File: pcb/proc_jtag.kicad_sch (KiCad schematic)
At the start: 3 parts

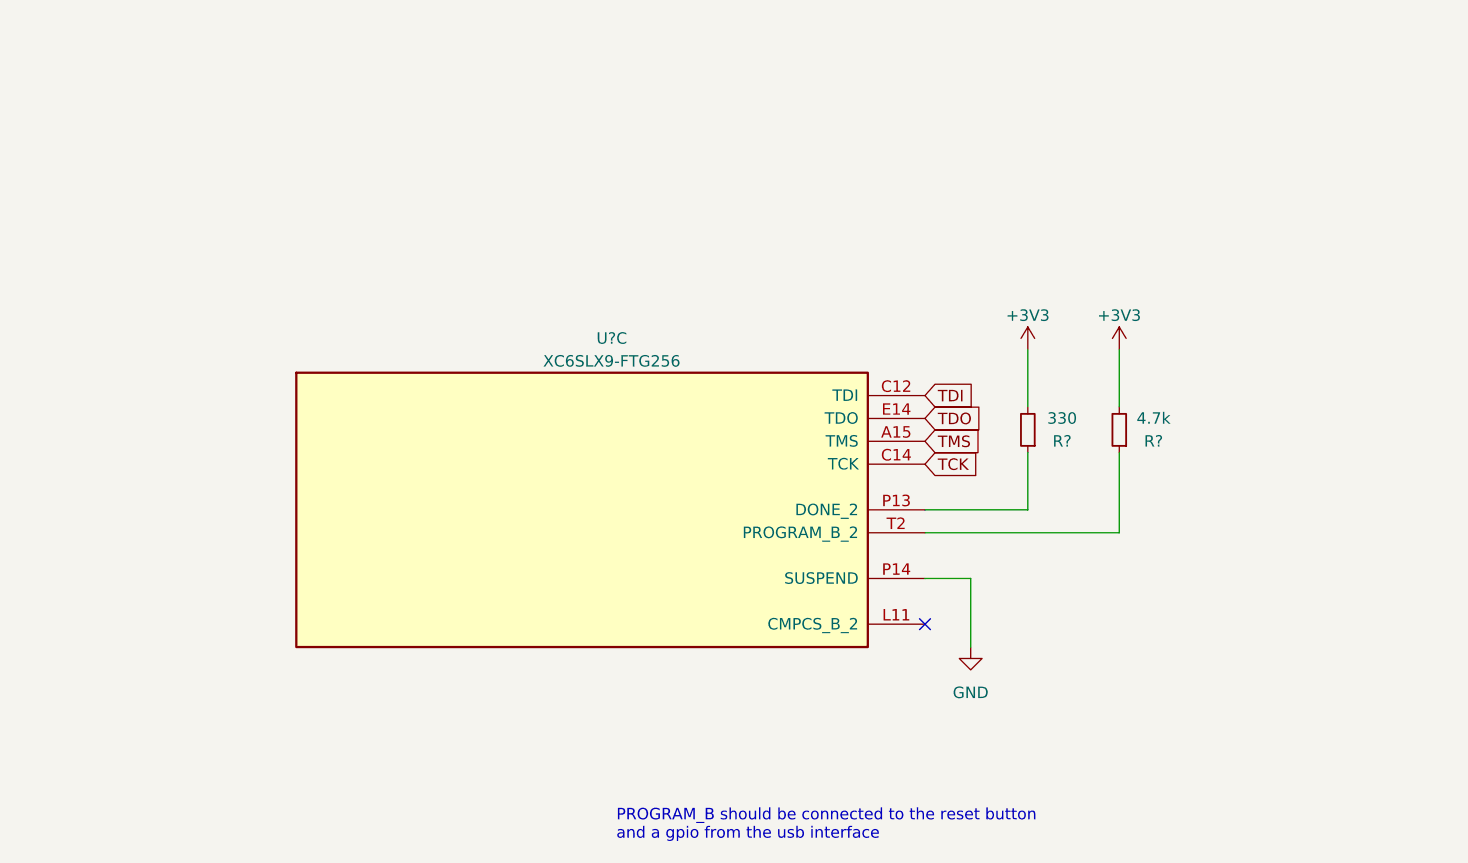
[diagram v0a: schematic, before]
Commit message: add flash memory
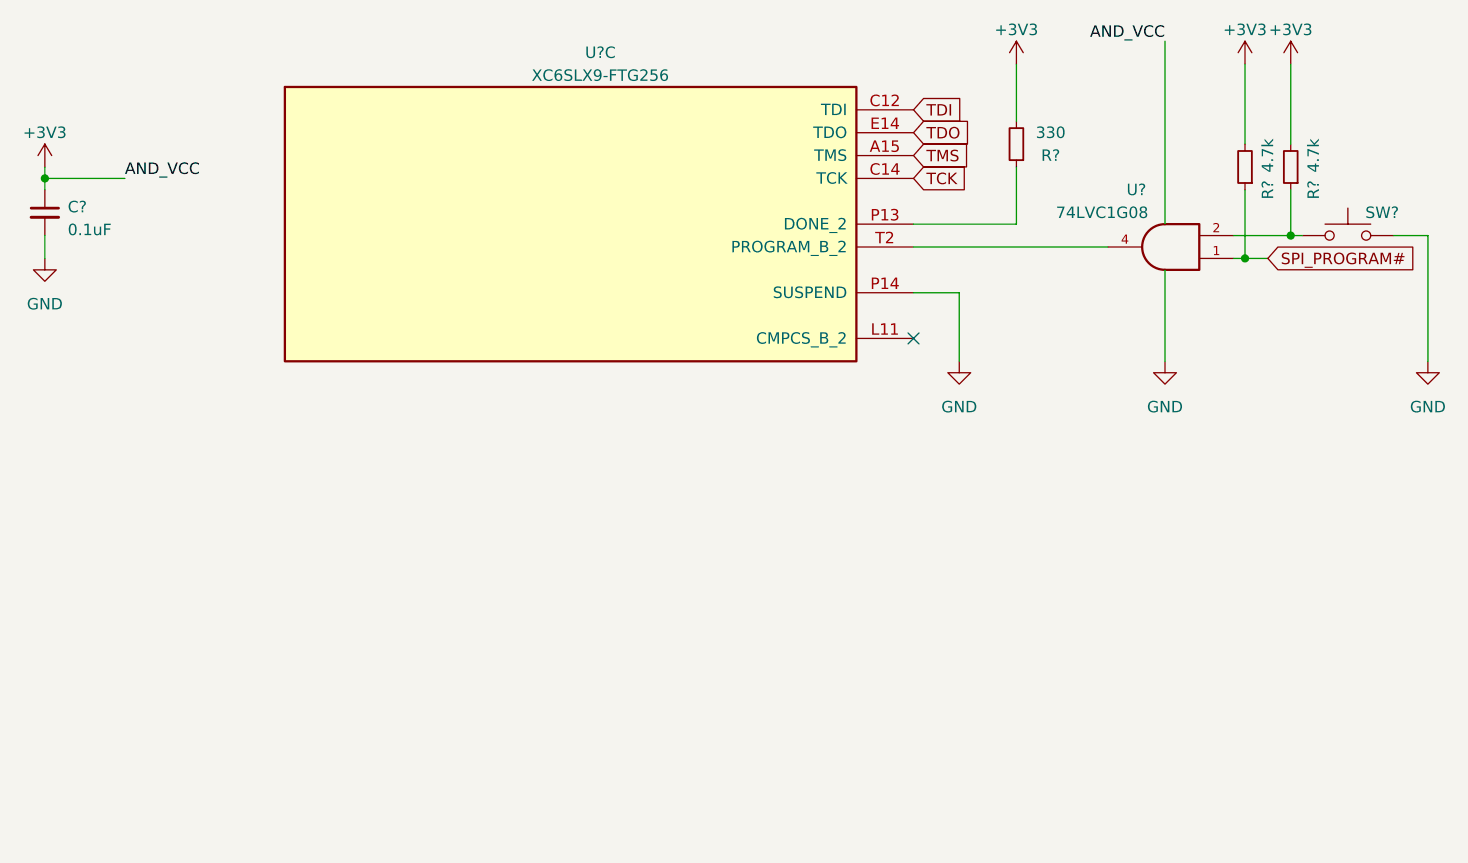
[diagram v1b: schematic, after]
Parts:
- removed R?: 4.7k, symbol Device:R_Small
- added C?: 0.1uF, symbol Device:C_Small
- added R? (x2): 4.7k, symbol Device:R_Small
- added SW?: SW_Push, symbol Switch:SW_Push
- added U?: 74LVC1G08, symbol 74xGxx:74LVC1G08
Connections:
- net GND is gone; now on net +3V3: U?.P14 (SUSPEND)
- net +3V3: now also C?.1, C?.2, R?.2, R?.2, SW?.2, U?.3 (GND), U?.5 (VCC)
- net at U?.T2 (PROGRAM_B_2): now also U?.4
- new net: R?.1, SW?.1, U?.2
- new net SPI_PROGRAM#: R?.1, U?.1
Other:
- note removed: "PROGRAM_B should be connected to the reset button and a gpio from the usb interface"
- moved on the sheet: R?, U?C

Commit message: add the din connector
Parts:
- removed U?: XC6SLX9-FTG256, symbol FPGA_Xilinx_Spartan6:XC6SLX9-FTG256
- added U?: XC6SLX16-FTG256, symbol FPGA_Xilinx_Spartan6:XC6SLX16-FTG256
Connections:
- net +3V3: now also U?.P14 (SUSPEND)
- net TCK: now also U?.C14 (TCK)
- net TDI: now also U?.C12 (TDI)
- net TDO: now also U?.E14 (TDO)
- net TMS: now also U?.A15 (TMS)
- net at R?.1: now also U?.P13 (DONE_2)
- net at U?.4: now also U?.T2 (PROGRAM_B_2)
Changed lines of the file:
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@@
     (pin "5")
   )
-  (symbol (lib_id "FPGA_Xilinx_Spartan6:XC6SLX9-FTG256") (at 82.55 53.34 0) (unit 3)
+  (symbol (lib_id "FPGA_Xilinx_Spartan6:XC6SLX16-FTG256") (at 82.55 53.34 0) (unit 3)
     (in_bom yes) (on_board yes) (fields_autoplaced)
     (property "Reference" "U?" (id 0) (at 85.852 34.29 0))
-    (property "Value" "XC6SLX9-FTG256" (id 1) (at 85.852 36.83 0))
+    (property "Value" "XC6SLX16-FTG256" (id 1) (at 85.852 36.83 0))
     (property "Footprint" "" (id 2) (at 82.55 53.34 0)
       (effects (font (size 1.27 1.27)) hide)

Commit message: start associating footprints
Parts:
- C71: renamed from C?; footprint (none) -> Capacitor_SMD:C_0402_1005Metric
- gave numbers to parts that had none: 6
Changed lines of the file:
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@@
   (symbol (lib_id "power:+3V3") (at 24.13 46.99 0) (unit 1)
     (in_bom yes) (on_board yes) (fields_autoplaced)
-    (property "Reference" "#PWR?" (id 0) (at 24.13 50.8 0)
+    (property "Reference" "#PWR093" (id 0) (at 24.13 50.8 0)
       (effects (font (size 1.27 1.27)) hide)
     )
@@
   (symbol (lib_id "power:+3V3") (at 132.08 35.56 0) (unit 1)
     (in_bom yes) (on_board yes) (fields_autoplaced)
-    (property "Reference" "#PWR?" (id 0) (at 132.08 39.37 0)
+    (property "Reference" "#PWR090" (id 0) (at 132.08 39.37 0)
       (effects (font (size 1.27 1.27)) hide)
     )
@@
   (symbol (lib_id "power:+3V3") (at 157.48 35.56 0) (unit 1)
     (in_bom yes) (on_board yes) (fields_autoplaced)
-    (property "Reference" "#PWR?" (id 0) (at 157.48 39.37 0)
+    (property "Reference" "#PWR091" (id 0) (at 157.48 39.37 0)
       (effects (font (size 1.27 1.27)) hide)
     )
@@
   (symbol (lib_id "power:+3V3") (at 162.56 35.56 0) (unit 1)
     (in_bom yes) (on_board yes) (fields_autoplaced)
-    (property "Reference" "#PWR?" (id 0) (at 162.56 39.37 0)
+    (property "Reference" "#PWR092" (id 0) (at 162.56 39.37 0)
       (effects (font (size 1.27 1.27)) hide)
     )
@@
   (symbol (lib_id "power:GND") (at 24.13 57.15 0) (unit 1)
     (in_bom yes) (on_board yes) (fields_autoplaced)
-    (property "Reference" "#PWR?" (id 0) (at 24.13 63.5 0)
+    (property "Reference" "#PWR094" (id 0) (at 24.13 63.5 0)
       (effects (font (size 1.27 1.27)) hide)
     )
@@
   (symbol (lib_id "power:GND") (at 125.73 68.58 0) (unit 1)
     (in_bom yes) (on_board yes) (fields_autoplaced)
-    (property "Reference" "#PWR?" (id 0) (at 125.73 74.93 0)
+    (property "Reference" "#PWR095" (id 0) (at 125.73 74.93 0)
       (effects (font (size 1.27 1.27)) hide)
     )
@@
   (symbol (lib_id "power:GND") (at 148.59 68.58 0) (unit 1)
     (in_bom yes) (on_board yes) (fields_autoplaced)
-    (property "Reference" "#PWR?" (id 0) (at 148.59 74.93 0)
+    (property "Reference" "#PWR096" (id 0) (at 148.59 74.93 0)
       (effects (font (size 1.27 1.27)) hide)
     )
@@
   (symbol (lib_id "power:GND") (at 177.8 68.58 0) (unit 1)
     (in_bom yes) (on_board yes) (fields_autoplaced)
-    (property "Reference" "#PWR?" (id 0) (at 177.8 74.93 0)
+    (property "Reference" "#PWR097" (id 0) (at 177.8 74.93 0)
       (effects (font (size 1.27 1.27)) hide)
     )
@@
   (symbol (lib_id "Device:R_Small") (at 132.08 44.45 180) (unit 1)
     (in_bom yes) (on_board yes)
-    (property "Reference" "R?" (id 0) (at 135.89 45.72 0))
+    (property "Reference" "R33" (id 0) (at 135.89 45.72 0))
     (property "Value" "330" (id 1) (at 135.89 43.18 0))
     (property "Footprint" "" (id 2) (at 132.08 44.45 0)
@@
   (symbol (lib_id "Device:R_Small") (at 157.48 46.99 180) (unit 1)
     (in_bom yes) (on_board yes)
-    (property "Reference" "R?" (id 0) (at 160.02 49.53 90))
+    (property "Reference" "R34" (id 0) (at 160.02 49.53 90))
     (property "Value" "4.7k" (id 1) (at 160.02 45.72 90))
     (property "Footprint" "" (id 2) (at 157.48 46.99 0)
@@
   (symbol (lib_id "Device:R_Small") (at 162.56 46.99 180) (unit 1)
     (in_bom yes) (on_board yes)
-    (property "Reference" "R?" (id 0) (at 165.1 49.53 90))
+    (property "Reference" "R35" (id 0) (at 165.1 49.53 90))
     (property "Value" "4.7k" (id 1) (at 165.1 45.72 90))
     (property "Footprint" "" (id 2) (at 162.56 46.99 0)
@@
   (symbol (lib_id "Device:C_Small") (at 24.13 52.07 0) (unit 1)
     (in_bom yes) (on_board yes) (fields_autoplaced)
-    (property "Reference" "C?" (id 0) (at 26.67 51.4349 0)
+    (property "Reference" "C71" (id 0) (at 26.67 51.4349 0)
       (effects (font (size 1.27 1.27)) (justify left))
     )
@@
       (effects (font (size 1.27 1.27)) (justify left))
     )
-    (property "Footprint" "" (id 2) (at 24.13 52.07 0)
+    (property "Footprint" "Capacitor_SMD:C_0402_1005Metric" (id 2) (at 24.13 52.07 0)
       (effects (font (size 1.27 1.27)) hide)
     )
@@
   (symbol (lib_id "Switch:SW_Push") (at 168.91 54.61 0) (unit 1)
     (in_bom yes) (on_board yes)
-    (property "Reference" "SW?" (id 0) (at 172.72 52.07 0))
+    (property "Reference" "SW1" (id 0) (at 172.72 52.07 0))
     (property "Value" "SW_Push" (id 1) (at 168.91 50.8 0)
       (effects (font (size 1.27 1.27)) hide)
@@
   (symbol (lib_id "74xGxx:74LVC1G08") (at 148.59 55.88 180) (unit 1)
     (in_bom yes) (on_board yes)
-    (property "Reference" "U?" (id 0) (at 145.415 49.53 0))
+    (property "Reference" "U11" (id 0) (at 145.415 49.53 0))
     (property "Value" "74LVC1G08" (id 1) (at 141.605 52.07 0))
     (property "Footprint" "" (id 2) (at 148.59 55.88 0)
@@
   (symbol (lib_id "FPGA_Xilinx_Spartan6:XC6SLX16-FTG256") (at 82.55 53.34 0) (unit 3)
     (in_bom yes) (on_board yes) (fields_autoplaced)
-    (property "Reference" "U?" (id 0) (at 85.852 34.29 0))
+    (property "Reference" "U1" (id 0) (at 85.852 34.29 0))
     (property "Value" "XC6SLX16-FTG256" (id 1) (at 85.852 36.83 0))
     (property "Footprint" "" (id 2) (at 82.55 53.34 0)

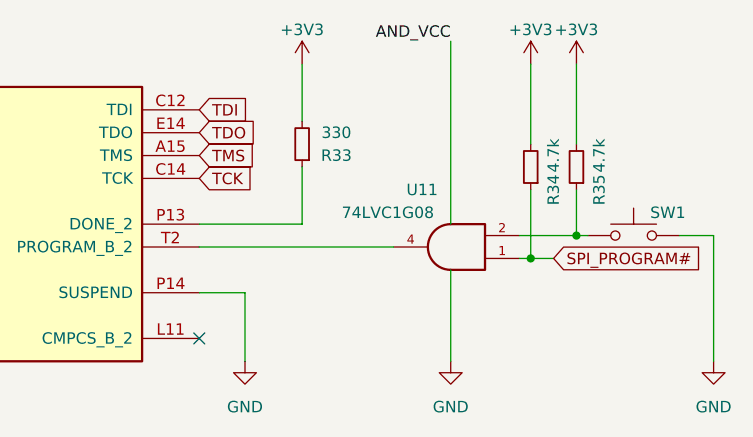
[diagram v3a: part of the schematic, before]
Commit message: add tps541620 footprint
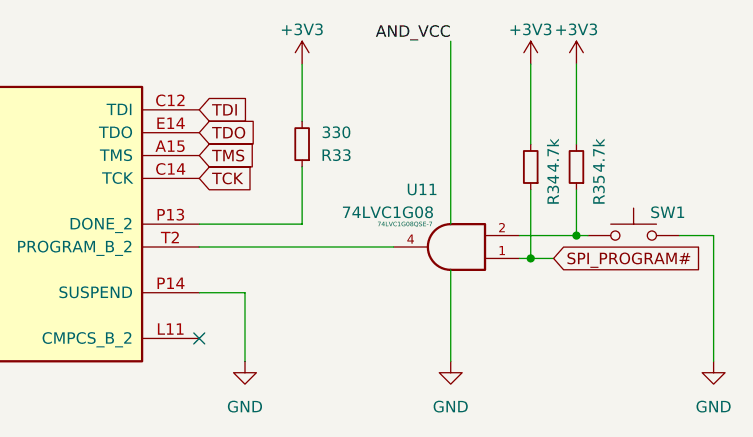
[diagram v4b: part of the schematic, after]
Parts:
- R33, R34, R35: footprint (none) -> Resistor_SMD:R_0402_1005Metric
- U1: footprint (none) -> Package_BGA:Xilinx_FTG256
- U11: footprint (none) -> Package_TO_SOT_SMD:SOT-353_SC-70-5; Ref (none) -> 74LVC1G08QSE-7
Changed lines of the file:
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@@
     (property "Reference" "R33" (id 0) (at 135.89 45.72 0))
     (property "Value" "330" (id 1) (at 135.89 43.18 0))
-    (property "Footprint" "" (id 2) (at 132.08 44.45 0)
+    (property "Footprint" "Resistor_SMD:R_0402_1005Metric" (id 2) (at 132.08 44.45 0)
       (effects (font (size 1.27 1.27)) hide)
     )
@@
     (property "Reference" "R34" (id 0) (at 160.02 49.53 90))
     (property "Value" "4.7k" (id 1) (at 160.02 45.72 90))
-    (property "Footprint" "" (id 2) (at 157.48 46.99 0)
+    (property "Footprint" "Resistor_SMD:R_0402_1005Metric" (id 2) (at 157.48 46.99 0)
       (effects (font (size 1.27 1.27)) hide)
     )
@@
     (property "Reference" "R35" (id 0) (at 165.1 49.53 90))
     (property "Value" "4.7k" (id 1) (at 165.1 45.72 90))
-    (property "Footprint" "" (id 2) (at 162.56 46.99 0)
+    (property "Footprint" "Resistor_SMD:R_0402_1005Metric" (id 2) (at 162.56 46.99 0)
       (effects (font (size 1.27 1.27)) hide)
     )
@@
     (property "Reference" "U11" (id 0) (at 145.415 49.53 0))
     (property "Value" "74LVC1G08" (id 1) (at 141.605 52.07 0))
-    (property "Footprint" "" (id 2) (at 148.59 55.88 0)
+    (property "Footprint" "Package_TO_SOT_SMD:SOT-353_SC-70-5" (id 2) (at 148.59 55.88 0)
       (effects (font (size 1.27 1.27)) hide)
     )
     (property "Datasheet" "http://www.ti.com/lit/sg/scyt129e/scyt129e.pdf" (id 3) (at 148.59 55.88 0)
       (effects (font (size 1.27 1.27)) hide)
+    )
+    (property "Ref" "74LVC1G08QSE-7" (id 4) (at 143.51 53.34 0)
+      (effects (font (size 0.5 0.5)))
     )
     (pin "1")
@@
     (property "Reference" "U1" (id 0) (at 85.852 34.29 0))
     (property "Value" "XC6SLX16-FTG256" (id 1) (at 85.852 36.83 0))
-    (property "Footprint" "" (id 2) (at 82.55 53.34 0)
+    (property "Footprint" "Package_BGA:Xilinx_FTG256" (id 2) (at 82.55 53.34 0)
       (effects (font (size 1.27 1.27)) hide)
     )

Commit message: add the front led glue logic
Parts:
- added D3: LED_Dual_AKA, symbol Device:LED_Dual_AKA
- added R36, R37: 52, symbol Device:R
- added R38, R39: A calculer, symbol Device:R
- added U15: BCM56DS, symbol bcm56ds:BCM56DS
- added U16: 74LS32, symbol 74xx:74LS32
- added U17: 74LS04, symbol 74xx:74LS04
- added U18: 74LS08, symbol 74xx:74LS08
- added U19: NE555P, symbol Timer:NE555P
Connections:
- net +3V3: now also D3.2 (K), U15.3 (C), U15.6 (C)
- net DONE: now reaches R33.1, U1.P13 (DONE_2)
- net DONE: now also U17.3, U18.1
- net PROGRAM_B#: now reaches U1.T2 (PROGRAM_B_2), U11.4
- net PROGRAM_B#: now also U17.1
- new net: U16.3, U18.10
- new net: R39.2, U18.8
- new net: U17.6, U18.9
- new net: R36.1, U15.5 (E)
- new net: D3.1 (A1), R36.2
- new net: U16.1, U18.6
- new net: U16.2, U19.3 (Q)
- new net: R38.2, U15.1 (B)
- new net: D3.3 (A2), R37.1
- new net: R38.1, U17.5, U18.3
- new net: R39.1, U15.2 (B)
- new net: R37.2, U15.4 (E)
- new net: U17.2, U18.2, U18.4
- new net: U17.4, U18.5
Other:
- note added: "BCM56DS's DC gain is 63 minimum. In order to get at least 30mA of current, we need a base current of 0.5mA."
- note added: "GREEN"
- note added: "Green = Done & !INIT_B# Orange = (Blink | (!DONE && !INIT_B#)) & !Green"
- note added: "ORANGE"
- note added: "These LEDs have a forward voltage from 2V to 2.5V, rated at 20mA. 52ohms gives 25mA at a forward voltage of 2V and 15mA at 2.5V."
- moved on the sheet: R33, R34, R35, SW1, U11, U1C
